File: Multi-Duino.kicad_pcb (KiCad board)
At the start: 4 copper layers, 68.6 x 53.3 mm, 67 parts, among them J1 M20-9980345, J10 Micro_SD_Card_Det1, J2 M20-9980245, J3 M20-9980345, J4 PPTC101LFBN-RC, J5 PPTC081LFBN-RC, J6 PPTC061LFBN-RC, J7 PPTC081LFBN-RC, J8 USB_C_Receptacle_USB2.0_16P, Q1 FDN340P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

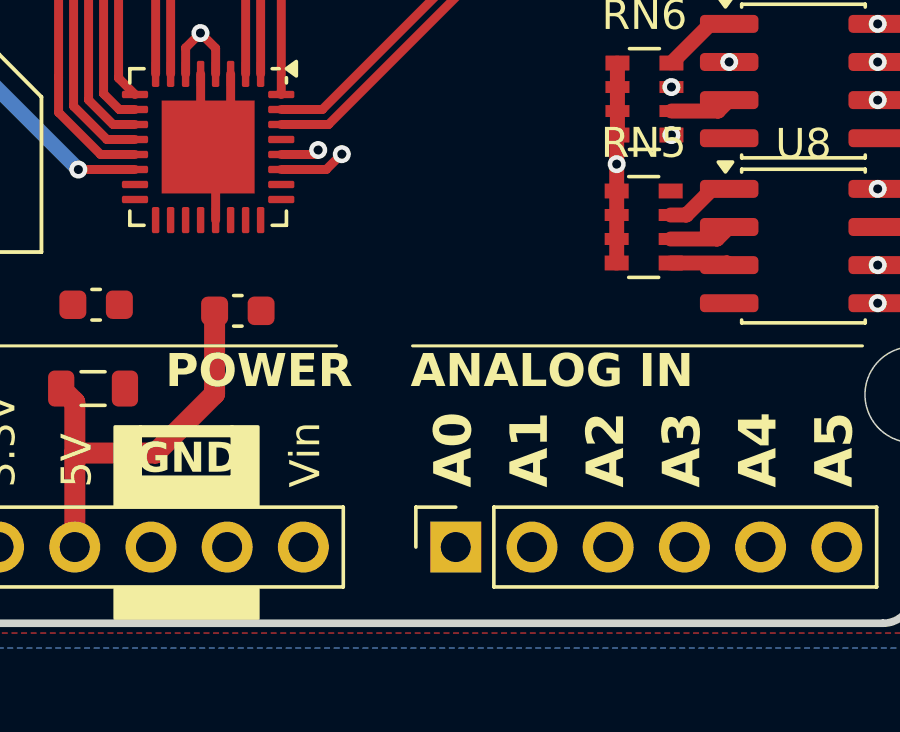
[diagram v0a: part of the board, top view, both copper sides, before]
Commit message: Update Multiduino v2 design
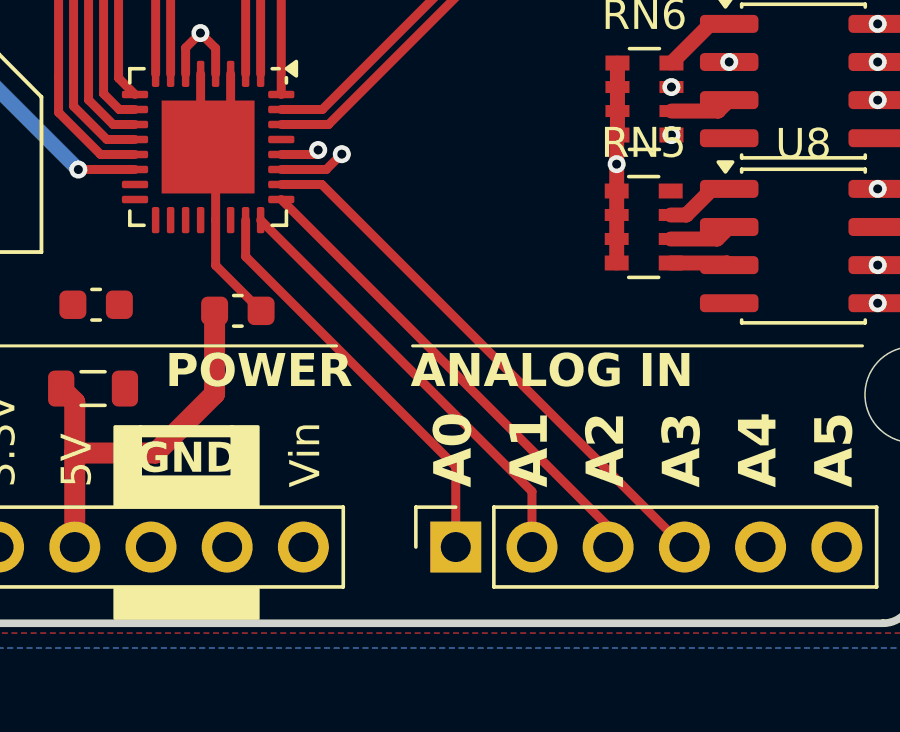
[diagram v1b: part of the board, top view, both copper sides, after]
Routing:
- net A3: track 0.00 -> 18.4 mm
- net A2: track 0.00 -> 16.1 mm
- net A1: track 0.00 -> 14.6 mm
- net A0: track 0.00 -> 13.8 mm
- net GND: track 7.83 -> 11.5 mm
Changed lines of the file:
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@@
+	)
+	(segment
+		(start 157.0061 119.744)
+		(end 158.5217 121.2596)
+		(width 0.3)
+		(layer "F.Cu")
+		(net 1)
 	)
 	(segment
@@
 		(start 157.5061 113.3611)
 		(end 157.5061 115.0486)
+		(width 0.3)
+		(layer "F.Cu")
+		(net 1)
+	)
+	(segment
+		(start 157.0061 118.2361)
+		(end 157.0061 119.744)
 		(width 0.3)
 		(layer "F.Cu")
@@
 	)
 	(segment
+		(start 159.1936 117.5486)
+		(end 170.091 128.446)
+		(width 0.3)
+		(layer "F.Cu")
+		(net 46)
+	)
+	(segment
+		(start 170.091 128.446)
+		(end 170.091 129.1336)
+		(width 0.3)
+		(layer "F.Cu")
+		(net 46)
+	)
+	(segment
+		(start 158.0061 118.2361)
+		(end 158.0061 119.449592)
+		(width 0.3)
+		(layer "F.Cu")
+		(net 47)
+	)
+	(segment
+		(start 158.0061 119.449592)
+		(end 165.011 126.454492)
+		(width 0.3)
+		(layer "F.Cu")
+		(net 47)
+	)
+	(segment
+		(start 165.011 126.454492)
+		(end 165.011 129.1336)
+		(width 0.3)
+		(layer "F.Cu")
+		(net 47)
+	)
+	(segment
+		(start 158.5061 118.2361)
+		(end 167.551 127.281)
+		(width 0.3)
+		(layer "F.Cu")
+		(net 48)
+	)
+	(segment
+		(start 167.551 127.281)
+		(end 167.551 129.1336)
+		(width 0.3)
+		(layer "F.Cu")
+		(net 48)
+	)
+	(segment
+		(start 160.546 117.0486)
+		(end 172.631 129.1336)
+		(width 0.3)
+		(layer "F.Cu")
+		(net 49)
+	)
+	(segment
+		(start 159.1936 117.0486)
+		(end 160.546 117.0486)
+		(width 0.3)
+		(layer "F.Cu")
+		(net 49)
+	)
+	(segment

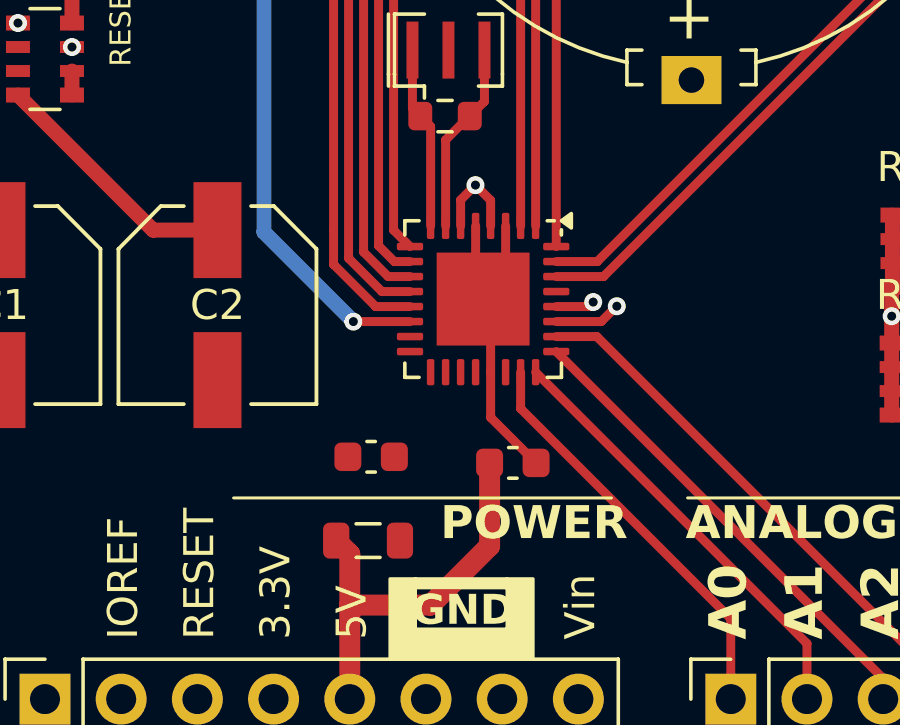
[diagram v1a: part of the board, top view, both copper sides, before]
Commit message: Update Multiduino v2 design
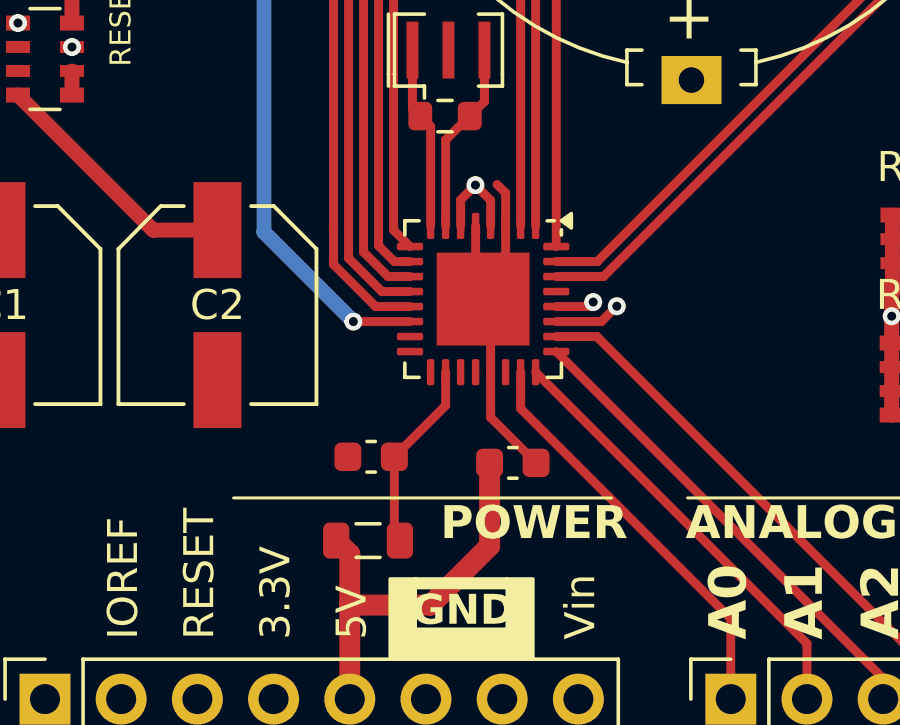
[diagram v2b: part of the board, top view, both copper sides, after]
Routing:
- net AVCC: track 0.00 -> 6.40 mm
- net GND: track 11.5 -> 13.0 mm
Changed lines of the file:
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@@
+	)
+	(segment
+		(start 157.5061 113.3611)
+		(end 157.5061 112.2661)
+		(width 0.3)
+		(layer "F.Cu")
+		(net 1)
 	)
 	(segment
 		(start 156.5061 115.5486)
 		(end 156.7561 115.7986)
+		(width 0.3)
+		(layer "F.Cu")
+		(net 1)
+	)
+	(segment
+		(start 157.5061 112.2661)
+		(end 157.22 111.98)
 		(width 0.3)
 		(layer "F.Cu")
@@
 	)
 	(segment
+		(start 153.7973 123.6645)
+		(end 153.9832 123.8504)
+		(width 0.3)
+		(layer "F.Cu")
+		(net 10)
+	)
+	(segment
+		(start 155.5061 119.3476)
+		(end 153.7973 121.0564)
+		(width 0.3)
+		(layer "F.Cu")
+		(net 10)
+	)
+	(segment
+		(start 153.7973 121.0564)
+		(end 153.7973 123.6645)
+		(width 0.3)
+		(layer "F.Cu")
+		(net 10)
+	)
+	(segment
+		(start 155.5061 118.2361)
+		(end 155.5061 119.3476)
+		(width 0.3)
+		(layer "F.Cu")
+		(net 10)
+	)
+	(segment
 		(start 132.9001 99.4401)
 		(end 132.9001 100.8966)
@@
 		(hatch none 0.5)
 		(connect_pads yes
-			(clearance 0.3)
+			(clearance 0.25)
 		)
 		(min_thickness 0.25)
@@
 		(hatch none 0.5)
 		(connect_pads yes
-			(clearance 0.3)
+			(clearance 0.25)
 		)
 		(min_thickness 0.25)
@@
 		(hatch none 0.5)
 		(connect_pads yes
-			(clearance 0.3)
+			(clearance 0.25)
 		)
 		(min_thickness 0.25)
@@
 		(hatch none 0.5)
 		(connect_pads yes
-			(clearance 0.3)
+			(clearance 0.25)
 		)
 		(min_thickness 0.25)

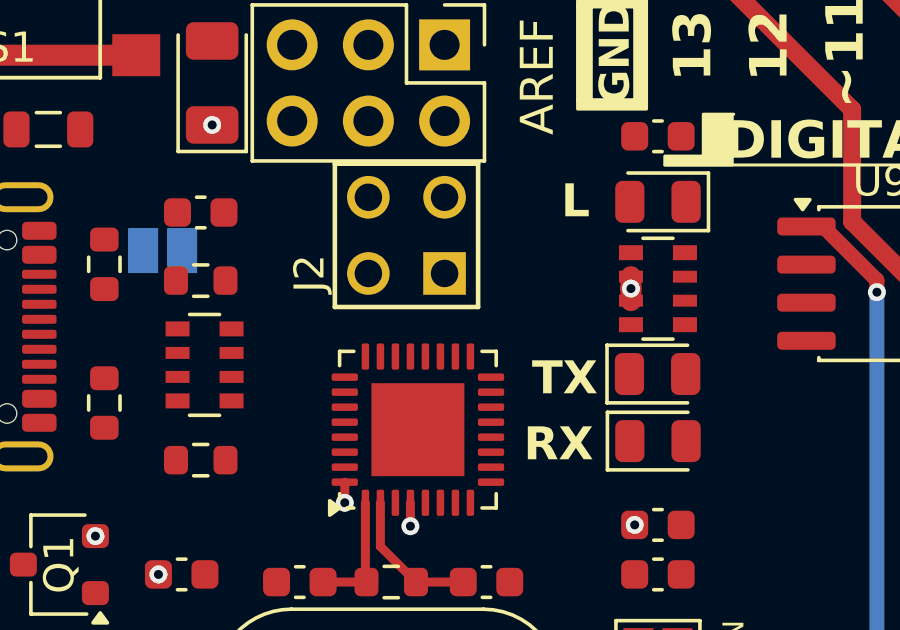
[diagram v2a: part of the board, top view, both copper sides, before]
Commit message: Update Multiduino v2 design
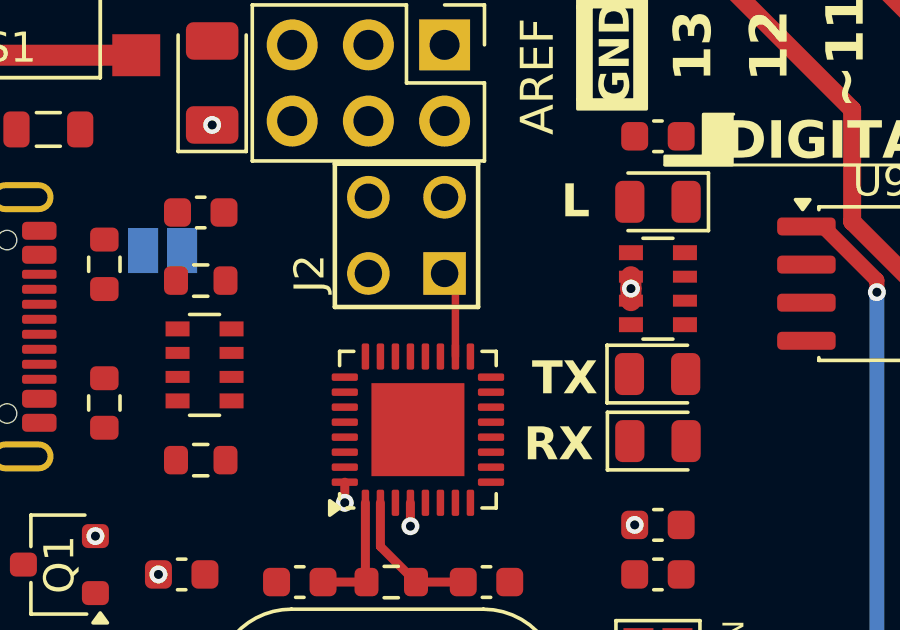
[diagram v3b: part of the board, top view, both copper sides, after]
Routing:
- net PB4: track 0.00 -> 2.92 mm
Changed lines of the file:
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@@
+	)
+	(segment
+		(start 135.4001 92.1571)
+		(end 135.039 91.796)
+		(width 0.25)
+		(layer "F.Cu")
+		(net 27)
+	)
+	(segment
+		(start 135.4001 94.5651)
+		(end 135.4001 92.1571)
+		(width 0.25)
+		(layer "F.Cu")
+		(net 27)
 	)
 	(segment

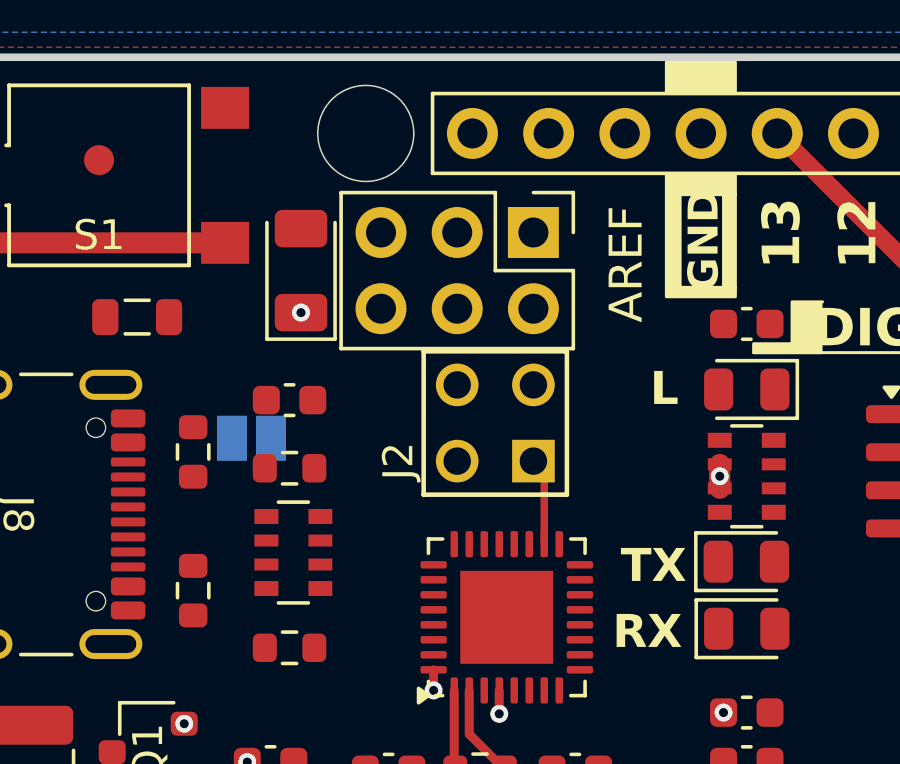
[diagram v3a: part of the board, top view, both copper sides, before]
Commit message: Update Multiduino v2 design
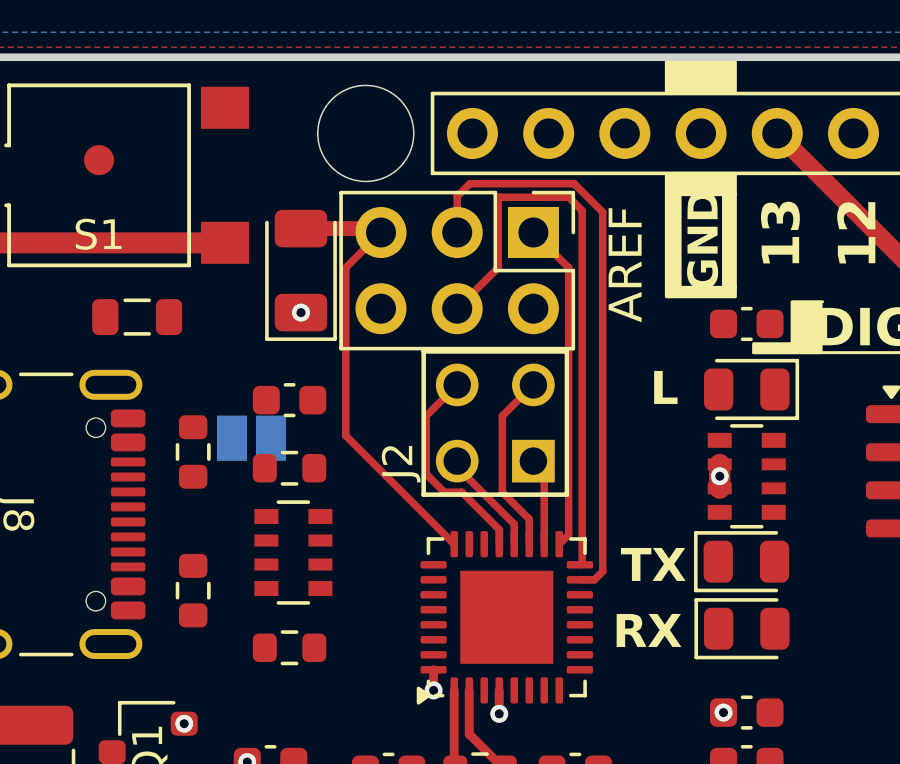
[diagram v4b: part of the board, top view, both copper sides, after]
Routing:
- net SCK2: track 0.00 -> 19.5 mm
- net MOSI2: track 0.00 -> 19.1 mm
- net RESET2: track 0.00 -> 15.1 mm
- net MISO2: track 0.00 -> 11.0 mm
- net PB7: track 0.00 -> 7.09 mm
- net PB5: track 0.00 -> 6.11 mm
- net PB6: track 0.00 -> 3.56 mm
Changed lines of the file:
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@@
+	)
+	(segment
+		(start 129.8291 84.0456)
+		(end 129.9591 84.1756)
+		(width 0.5)
+		(layer "F.Cu")
+		(net 13)
+	)
+	(segment
+		(start 127.2921 84.0456)
+		(end 129.8291 84.0456)
+		(width 0.5)
+		(layer "F.Cu")
+		(net 13)
+	)
+	(segment
+		(start 128.7841 90.9491)
+		(end 128.7841 85.3506)
+		(width 0.25)
+		(layer "F.Cu")
+		(net 13)
+	)
+	(segment
+		(start 128.7841 85.3506)
+		(end 129.9591 84.1756)
+		(width 0.25)
+		(layer "F.Cu")
+		(net 13)
+	)
+	(segment
+		(start 132.4001 94.5651)
+		(end 128.7841 90.9491)
+		(width 0.25)
+		(layer "F.Cu")
+		(net 13)
 	)
 	(segment
@@
 	)
 	(segment
+		(start 136.5876 95.7526)
+		(end 137.07484 95.7526)
+		(width 0.25)
+		(layer "F.Cu")
+		(net 23)
+	)
+	(segment
+		(start 136.400496 82.5506)
+		(end 132.922019 82.5506)
+		(width 0.25)
+		(layer "F.Cu")
+		(net 23)
+	)
+	(segment
+		(start 132.922019 82.5506)
+		(end 132.4991 82.973519)
+		(width 0.25)
+		(layer "F.Cu")
+		(net 23)
+	)
+	(segment
+		(start 137.3501 95.47734)
+		(end 137.3501 83.500204)
+		(width 0.25)
+		(layer "F.Cu")
+		(net 23)
+	)
+	(segment
+		(start 137.07484 95.7526)
+		(end 137.3501 95.47734)
+		(width 0.25)
+		(layer "F.Cu")
+		(net 23)
+	)
+	(segment
+		(start 137.3501 83.500204)
+		(end 136.400496 82.5506)
+		(width 0.25)
+		(layer "F.Cu")
+		(net 23)
+	)
+	(segment
+		(start 132.4991 82.973519)
+		(end 132.4991 84.1756)
+		(width 0.25)
+		(layer "F.Cu")
+		(net 23)
+	)
+	(segment
+		(start 133.8641 85.3506)
+		(end 132.4991 86.7156)
+		(width 0.25)
+		(layer "F.Cu")
+		(net 24)
+	)
+	(segment
+		(start 136.2141 83.0006)
+		(end 133.8641 83.0006)
+		(width 0.25)
+		(layer "F.Cu")
+		(net 24)
+	)
+	(segment
+		(start 136.6641 83.4506)
+		(end 136.2141 83.0006)
+		(width 0.25)
+		(layer "F.Cu")
+		(net 24)
+	)
+	(segment
+		(start 136.5876 95.2526)
+		(end 136.6641 95.1761)
+		(width 0.25)
+		(layer "F.Cu")
+		(net 24)
+	)
+	(segment
+		(start 133.8641 83.0006)
+		(end 133.8641 85.3506)
+		(width 0.25)
+		(layer "F.Cu")
+		(net 24)
+	)
+	(segment
+		(start 136.6641 95.1761)
+		(end 136.6641 83.4506)
+		(width 0.25)
+		(layer "F.Cu")
+		(net 24)
+	)
+	(segment
+		(start 136.2141 94.2511)
+		(end 136.2141 85.3506)
+		(width 0.25)
+		(layer "F.Cu")
+		(net 25)
+	)
+	(segment
+		(start 135.9001 94.5651)
+		(end 136.2141 94.2511)
+		(width 0.25)
+		(layer "F.Cu")
+		(net 25)
+	)
+	(segment
+		(start 136.2141 85.3506)
+		(end 135.0391 84.1756)
+		(width 0.25)
+		(layer "F.Cu")
+		(net 25)
+	)
+	(segment
+		(start 134.9001 93.7295)
+		(end 134.0028 92.8322)
+		(width 0.25)
+		(layer "F.Cu")
+		(net 26)
+	)
+	(segment
+		(start 134.0028 90.2922)
+		(end 135.039 89.256)
+		(width 0.25)
+		(layer "F.Cu")
+		(net 26)
+	)
+	(segment
+		(start 134.9001 94.5651)
+		(end 134.9001 93.7295)
+		(width 0.25)
+		(layer "F.Cu")
+		(net 26)
+	)
+	(segment
+		(start 134.0028 92.8322)
+		(end 134.0028 90.2922)
+		(width 0.25)
+		(layer "F.Cu")
+		(net 26)
+	)
+	(segment
 		(start 135.4001 92.1571)
 		(end 135.039 91.796)
@@
 	)
 	(segment
+		(start 133.9001 94.5651)
+		(end 133.9001 94.07786)
+		(width 0.25)
+		(layer "F.Cu")
+		(net 28)
+	)
+	(segment
+		(start 133.9001 94.07786)
+		(end 132.65444 92.8322)
+		(width 0.25)
+		(layer "F.Cu")
+		(net 28)
+	)
+	(segment
+		(start 131.4628 90.2922)
+		(end 132.499 89.256)
+		(width 0.25)
+		(layer "F.Cu")
+		(net 28)
+	)
+	(segment
+		(start 132.65444 92.8322)
+		(end 132.069791 92.8322)
+		(width 0.25)
+		(layer "F.Cu")
+		(net 28)
+	)
+	(segment
+		(start 132.069791 92.8322)
+		(end 131.4628 92.225209)
+		(width 0.25)
+		(layer "F.Cu")
+		(net 28)
+	)
+	(segment
+		(start 131.4628 92.225209)
+		(end 131.4628 90.2922)
+		(width 0.25)
+		(layer "F.Cu")
+		(net 28)
+	)
+	(segment
+		(start 132.499 91.999)
+		(end 134.4001 93.9001)
+		(width 0.25)
+		(layer "F.Cu")
+		(net 29)
+	)
+	(segment
+		(start 132.499 91.796)
+		(end 132.499 91.999)
+		(width 0.25)
+		(layer "F.Cu")
+		(net 29)
+	)
+	(segment
+		(start 134.4001 93.9001)
+		(end 134.4001 94.5651)
+		(width 0.25)
+		(layer "F.Cu")
+		(net 29)
+	)
+	(segment

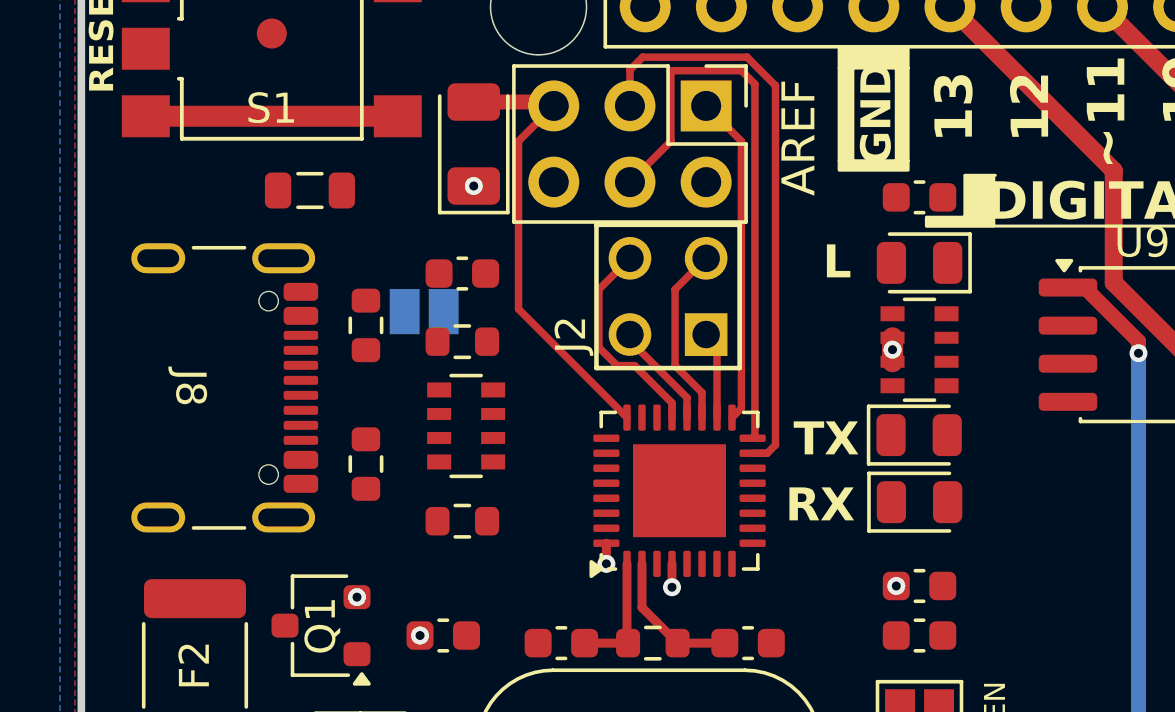
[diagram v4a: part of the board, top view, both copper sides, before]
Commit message: Update Multiduino v2 design
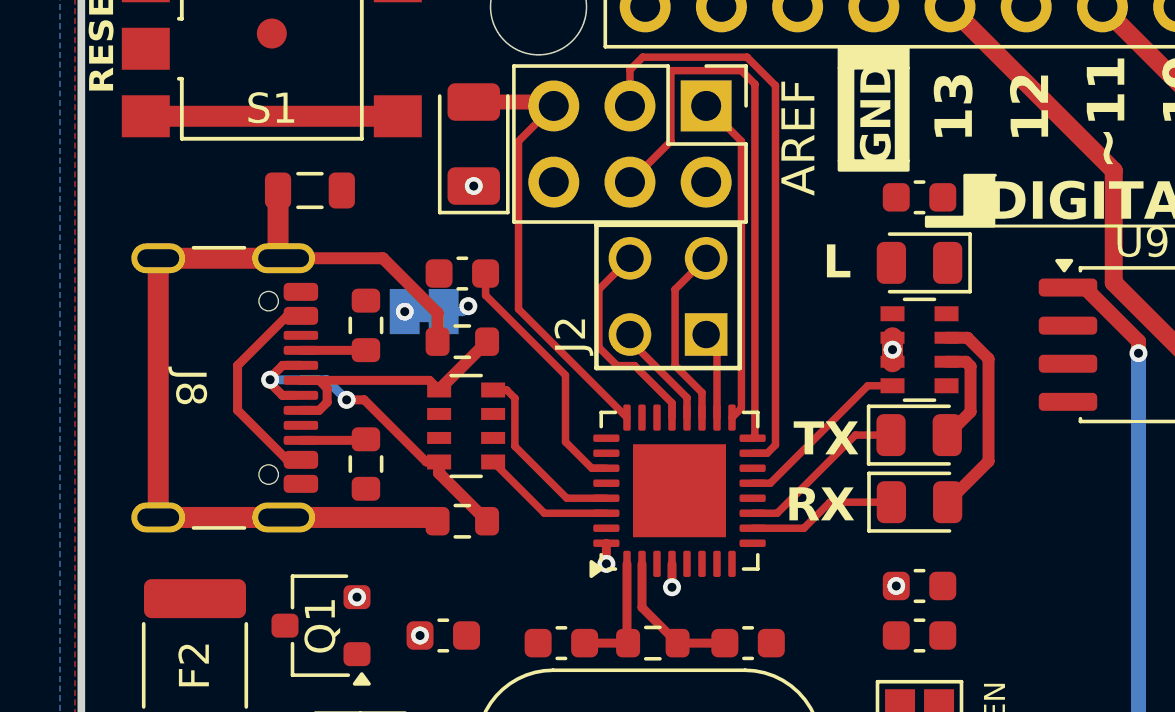
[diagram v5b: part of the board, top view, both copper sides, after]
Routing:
- net USHIELD: track 0.00 -> 31.4 mm
- net D-: track 0.00 -> 11.8 mm, vias 0 -> 2
- net D+: track 0.00 -> 9.45 mm
- net Net-(U3-UCAP): track 0.00 -> 8.44 mm
- net XUSB: track 0.00 -> 7.08 mm
- net Net-(D6-A): track 0.00 -> 7.03 mm
- net RD+: track 0.00 -> 6.21 mm
- net DTR: track 0.00 -> 6.01 mm
- net TXLED: track 0.00 -> 5.69 mm
- net RXLED: track 0.00 -> 4.99 mm
- net RD-: track 0.00 -> 4.48 mm
- net Net-(D5-A): track 0.00 -> 3.48 mm
- net GND: track 13.0 -> 15.2 mm, vias 0 -> 2
- net CC2: track 0.00 -> 2.18 mm
- net CC1: track 0.00 -> 2.17 mm
